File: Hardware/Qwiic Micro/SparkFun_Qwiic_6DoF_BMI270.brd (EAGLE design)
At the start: 7.6 x 19.1 mm, 45 parts, among them J1 QWIIC_RIGHT_ANGLE, U1 BMI270

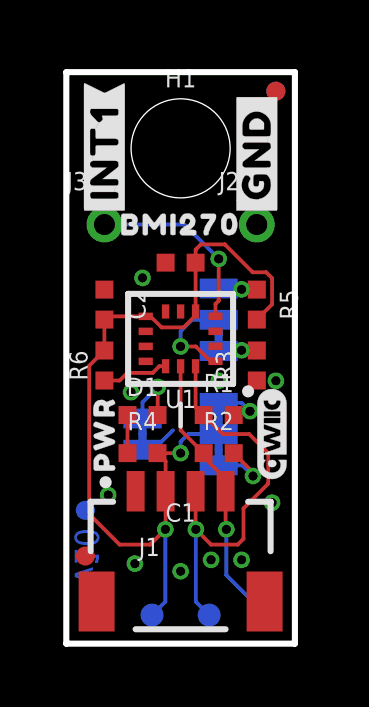
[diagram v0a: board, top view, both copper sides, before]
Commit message: Design review updates
Qwiic 1x1:
Add y position of headers to measures
Nudge I2C vias under right Qwiic connector
Nudge vias away from silk

Qwiic Micro:
Remove traces and vias under chip
Nudge via away from x-gyro arrowhead
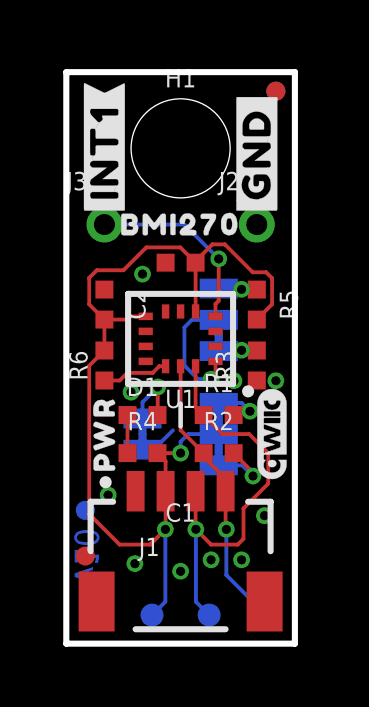
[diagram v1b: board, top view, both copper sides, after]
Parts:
- moved U$79 0.13 mm to (6.86, 3.56)
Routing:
- net 3.3V: track 28.7 -> 31.8 mm
- net ADR: track 3.30 -> 4.25 mm
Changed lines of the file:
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@@
 <rectangle x1="3.683" y1="3.683" x2="3.937" y2="3.937" layer="41"/>
 <rectangle x1="2.413" y1="7.62" x2="2.667" y2="7.874" layer="41"/>
+<rectangle x1="3.175" y1="10.541" x2="3.937" y2="10.795" layer="41"/>
 </plain>
 <attributes>
@@
 <element name="U$21" library="output" package="BMI2700" value="" x="3.81" y="13.97" smashed="yes"/>
 <element name="U$33" library="SparkFun-Aesthetics" package="ORDERING_INSTRUCTIONS" value="" x="15.24" y="50.8" smashed="yes"/>
-<element name="U$79" library="output" package="X0" value="" x="6.858" y="3.683" smashed="yes" rot="MR0"/>
+<element name="U$79" library="output" package="X0" value="" x="6.858" y="3.556" smashed="yes" rot="MR0"/>
 <element name="U$80" library="output" package="Y0" value="" x="3.683" y="3.048" smashed="yes" rot="MR0"/>
 <element name="U$81" library="output" package="Z0" value="" x="6.477" y="2.159" smashed="yes" rot="MR0"/>
@@
 <wire x1="4.31" y1="12.7" x2="4.31" y2="11.0725" width="0.127" layer="1"/>
 <contactref element="R6" pad="2"/>
-<wire x1="2.6475" y1="10.91" x2="1.29" y2="10.91" width="0.127" layer="1"/>
-<wire x1="1.29" y1="10.91" x2="1.163" y2="10.91" width="0.127" layer="1"/>
-<wire x1="1.163" y1="10.91" x2="1.27" y2="10.803" width="0.127" layer="1"/>
-<wire x1="1.27" y1="9.771" x2="1.27" y2="10.89" width="0.127" layer="1"/>
-<wire x1="1.27" y1="10.89" x2="1.29" y2="10.91" width="0.127" layer="1"/>
-<wire x1="2.6475" y1="10.91" x2="2.806" y2="10.91" width="0.127" layer="1"/>
-<wire x1="3.91040625" y1="10.541" x2="4.31" y2="10.94059375" width="0.127" layer="1"/>
-<wire x1="4.31" y1="10.94059375" x2="4.31" y2="11.0725" width="0.127" layer="1"/>
-<wire x1="2.806" y1="10.91" x2="3.175" y2="10.541" width="0.127" layer="1"/>
-<wire x1="3.175" y1="10.541" x2="3.91040625" y2="10.541" width="0.127" layer="1"/>
 <wire x1="6.858" y1="12.184" x2="6.858" y2="11.311" width="0.127" layer="1"/>
 <wire x1="6.35" y1="10.803" x2="6.858" y2="11.311" width="0.127" layer="1"/>
 <wire x1="6.858" y1="12.184" x2="6.6635" y2="12.3785" width="0.127" layer="1"/>
-<wire x1="5.2832" y1="13.3096" x2="4.4878" y2="13.3096" width="0.127" layer="1"/>
-<wire x1="4.4878" y1="13.3096" x2="4.31" y2="13.1318" width="0.127" layer="1"/>
-<wire x1="4.31" y1="13.1318" x2="4.31" y2="12.7" width="0.127" layer="1"/>
+<wire x1="5.2832" y1="13.3096" x2="4.8688" y2="13.3096" width="0.127" layer="1"/>
+<wire x1="4.8688" y1="13.3096" x2="4.31" y2="12.7508" width="0.127" layer="1"/>
+<wire x1="4.31" y1="12.7" x2="4.31" y2="12.7508" width="0.127" layer="1"/>
 <wire x1="6.6635" y1="12.3785" x2="6.2143" y2="12.3785" width="0.127" layer="1"/>
 <wire x1="6.2143" y1="12.3785" x2="5.2832" y2="13.3096" width="0.127" layer="1"/>
@@
 <wire x1="3.04" y1="6.35" x2="3.31" y2="6.08" width="0.127" layer="1"/>
 <wire x1="3.04" y1="6.35" x2="3.81" y2="6.35" width="0.127" layer="1"/>
+<wire x1="4.31" y1="12.7" x2="3.802" y2="13.208" width="0.127" layer="1"/>
+<wire x1="2.667" y1="13.208" x2="3.802" y2="13.208" width="0.127" layer="1"/>
+<wire x1="0.762" y1="12.192" x2="1.016" y2="12.446" width="0.127" layer="1"/>
+<wire x1="1.27" y1="9.771" x2="1.27" y2="10.803" width="0.127" layer="1"/>
+<wire x1="2.139" y1="10.91" x2="2.032" y2="10.803" width="0.127" layer="1"/>
+<wire x1="1.27" y1="10.803" x2="2.032" y2="10.803" width="0.127" layer="1"/>
+<wire x1="2.139" y1="10.91" x2="2.6475" y2="10.91" width="0.127" layer="1"/>
+<wire x1="0.762" y1="11.311" x2="1.27" y2="10.803" width="0.127" layer="1"/>
+<wire x1="0.762" y1="12.192" x2="0.762" y2="11.311" width="0.127" layer="1"/>
+<wire x1="1.016" y1="12.446" x2="1.905" y2="12.446" width="0.127" layer="1"/>
+<wire x1="1.905" y1="12.446" x2="2.667" y2="13.208" width="0.127" layer="1"/>
 </signal>
 <signal name="GND">
@@
 <wire x1="3.31" y1="11.0725" x2="3.302" y2="11.0805" width="0.127" layer="1"/>
 <contactref element="PWR" pad="1"/>
-<via x="2.54" y="12.192" extent="1-16" drill="0.3048"/>
+<via x="2.54" y="12.319" extent="1-16" drill="0.3048"/>
 <via x="2.159" y="8.382" extent="1-16" drill="0.3048"/>
 <wire x1="3.1623" y1="6.7183" x2="2.794" y2="6.7183" width="0.127" layer="16"/>
@@
 <via x="5.842" y="2.794" extent="1-16" drill="0.3048"/>
 <via x="2.286" y="2.667" extent="1-16" drill="0.3048"/>
-<via x="5.08" y="8.763" extent="1-16" drill="0.3048"/>
+<via x="5.588" y="8.763" extent="1-16" drill="0.3048"/>
 <via x="6.985" y="8.763" extent="1-16" drill="0.3048"/>
-<via x="6.858" y="4.699" extent="1-16" drill="0.3048"/>
+<via x="6.604" y="4.2672" extent="1-16" drill="0.3048"/>
 </signal>
 <signal name="ADR">
 <contactref element="U1" pad="1"/>
 <contactref element="ADR" pad="2"/>
-<wire x1="4.9725" y1="9.41" x2="4.814" y2="9.41" width="0.127" layer="1"/>
-<wire x1="4.318" y1="9.906" x2="3.81" y2="9.906" width="0.127" layer="1"/>
-<via x="3.81" y="9.906" extent="1-16" drill="0.3048"/>
-<wire x1="3.81" y1="9.906" x2="3.81" y2="10.414" width="0.127" layer="16"/>
+<wire x1="4.9725" y1="9.41" x2="4.9725" y2="8.9603" width="0.127" layer="1"/>
+<wire x1="4.826" y1="8.8138" x2="4.9725" y2="8.9603" width="0.127" layer="1"/>
+<via x="4.826" y="8.8138" extent="1-16" drill="0.3048"/>
+<wire x1="4.826" y1="8.8138" x2="4.3942" y2="8.8138" width="0.127" layer="16"/>
+<wire x1="4.3942" y1="8.8138" x2="3.937" y2="9.271" width="0.127" layer="16"/>
+<wire x1="3.937" y1="10.541" x2="3.937" y2="9.271" width="0.127" layer="16"/>
 <wire x1="4.191" y1="10.795" x2="5.08" y2="10.795" width="0.127" layer="16"/>
-<wire x1="4.814" y1="9.41" x2="4.318" y2="9.906" width="0.127" layer="1"/>
-<wire x1="3.81" y1="10.414" x2="4.191" y2="10.795" width="0.127" layer="16"/>
+<wire x1="4.191" y1="10.795" x2="3.937" y2="10.541" width="0.127" layer="16"/>
 </signal>
 <signal name="SCL">

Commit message: Design review updates
Add gap to linear axis silk to clarify gyro directions
Add GND via to Qwiic Micro
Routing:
- net GND: vias 10 -> 11
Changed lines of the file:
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@@
 Finish: Lead Free HASL</text>
 <circle x="5.334" y="2.159" radius="0.508" width="0.1524" layer="22"/>
-<wire x1="5.969" y1="4.953" x2="5.969" y2="3.048" width="0.1524" layer="22" style="shortdash"/>
-<wire x1="3.429" y1="4.191" x2="5.334" y2="4.191" width="0.1524" layer="22" style="shortdash"/>
+<wire x1="5.969" y1="4.064" x2="5.969" y2="3.048" width="0.1524" layer="22" style="shortdash"/>
 <polygon width="0.1524" layer="22">
 <vertex x="5.969" y="3.048"/>
@@
 <rectangle x1="2.413" y1="7.62" x2="2.667" y2="7.874" layer="41"/>
 <rectangle x1="3.175" y1="10.541" x2="3.937" y2="10.795" layer="41"/>
+<wire x1="5.969" y1="4.953" x2="5.969" y2="4.572" width="0.1524" layer="22" style="shortdash"/>
+<wire x1="4.318" y1="4.191" x2="5.334" y2="4.191" width="0.1524" layer="22" style="shortdash"/>
+<wire x1="3.429" y1="4.191" x2="3.81" y2="4.191" width="0.1524" layer="22" style="shortdash"/>
 </plain>
 <attributes>
@@
 <via x="6.985" y="8.763" extent="1-16" drill="0.3048"/>
 <via x="6.604" y="4.2672" extent="1-16" drill="0.3048"/>
+<via x="1.651" y="12.954" extent="1-16" drill="0.3048"/>
 </signal>
 <signal name="ADR">

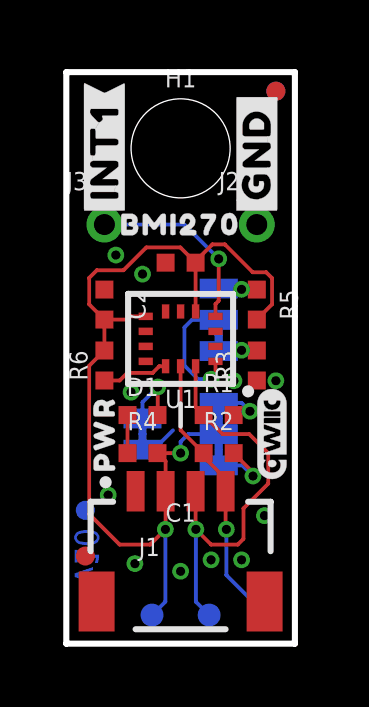
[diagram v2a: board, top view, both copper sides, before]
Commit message: Silk tweaks
Add silk lines between passive components
Nudge "BMI270" silk on Qwiic Micro
Add bigger pin 1 indicator dot to Qwiic Micro
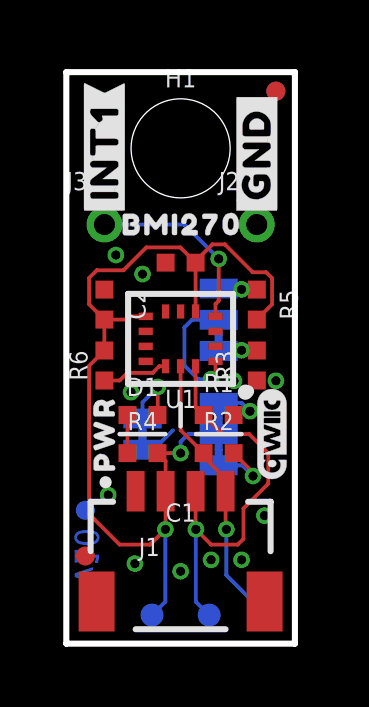
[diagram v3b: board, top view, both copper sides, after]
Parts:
- moved U$21 0.05 mm to (3.86, 14.0)
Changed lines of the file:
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@@
 <wire x1="4.318" y1="4.191" x2="5.334" y2="4.191" width="0.1524" layer="22" style="shortdash"/>
 <wire x1="3.429" y1="4.191" x2="3.81" y2="4.191" width="0.1524" layer="22" style="shortdash"/>
+<circle x="5.969" y="8.382" radius="0.127" width="0.254" layer="21"/>
+<wire x1="1.778" y1="6.985" x2="3.302" y2="6.985" width="0.1524" layer="21"/>
+<wire x1="4.318" y1="6.985" x2="5.842" y2="6.985" width="0.1524" layer="21"/>
 </plain>
 <attributes>
@@
 <element name="U$6" library="output" package="#0X68#0" value="" x="4.445" y="9.906" smashed="yes" rot="MR0"/>
 <element name="U$18" library="output" package="#0X69#0" value="" x="4.445" y="11.684" smashed="yes" rot="MR0"/>
-<element name="U$21" library="output" package="BMI2700" value="" x="3.81" y="13.97" smashed="yes"/>
+<element name="U$21" library="output" package="BMI2700" value="" x="3.8608" y="13.97" smashed="yes"/>
 <element name="U$33" library="SparkFun-Aesthetics" package="ORDERING_INSTRUCTIONS" value="" x="15.24" y="50.8" smashed="yes"/>
 <element name="U$79" library="output" package="X0" value="" x="6.858" y="3.556" smashed="yes" rot="MR0"/>
